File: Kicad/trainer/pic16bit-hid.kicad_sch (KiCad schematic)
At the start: 18 parts

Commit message: Update
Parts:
- BB401: renamed from BB?; value (none) -> BREADBOARD-170; footprint (none) -> tronixio:BREADBOARD-170
- EB401: value (none) -> EXPANSION-BOARD; footprint (none) -> tronixio:TRONIXIO-EXPANSION-BOARD
- JP401: value (none) -> VEE; footprint (none) -> tronixio:HARWIN-M20-999024x
- JP402: value (none) -> BCKL; footprint (none) -> tronixio:HARWIN-M20-999024x
- K401, K402: value (none) -> HARWIN-254-F-1X10-VERTICAL; footprint (none) -> tronixio:HARWIN-M20-782104x
- K409: value (none) -> HARWIN-254-F-1X16-VERTICAL; footprint (none) -> tronixio:HARWIN-M20-782164x
- LED401: value (none) -> KINGBRIGHT-DC10EWA; footprint (none) -> tronixio:KINGBRIGHT-DC
- P401: value (none) -> AN1; footprint (none) -> tronixio:PIHER-PT10MV
- P402: value (none) -> AN2; footprint (none) -> tronixio:PIHER-PT10MV
- R401: value (none) -> 5K; footprint (none) -> tronixio:PIHER-PT10LV
- R402: value (none) -> 10Ω; footprint (none) -> tronixio:RESISTOR-TH-1016
- RA401: value (none) -> 330Ω; footprint (none) -> tronixio:4611X
- S401: value (none) -> S1; footprint (none) -> tronixio:CK-KSA-TH
- S402: value (none) -> S3; footprint (none) -> tronixio:CK-KSA-TH
- S403: value (none) -> BOURNS-PEC12R-24DENTS; footprint (none) -> tronixio:BOURNS-PEC12R-SWITCH
- S404: value (none) -> S2; footprint (none) -> tronixio:CK-KSA-TH
- S405: value (none) -> S4; footprint (none) -> tronixio:CK-KSA-TH

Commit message: Update
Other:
- moved on the sheet: R401, R402

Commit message: Update Trainer
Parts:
- EB401: Name TRONIXIO-EXPANSION-BOARD -> (none)
- JP401, JP402: Name HARWIN-254-M-1X02-JUMPER-VERTICAL -> (none)
- K401, K402: Name HARWIN-254-F-1X10-VERTICAL -> (none)
- K409: Name HARWIN-254-F-1X16-VERTICAL -> (none)
- LED401: Name KINGBRIGHT-DC10EWA -> (none)
- P401, P402: Name PIHER-PT10MV-10K -> (none)
- R401: Name PIHER-PT10LV-5K -> (none)
- R402: Name RESISTOR-1016TH-10R -> (none)
- RA401: footprint tronixio:4611X -> tronixio:BOURNS-4611X; Name BOURNS-4611X-330R -> (none)
- S401, S402, S404, S405: Name CK-KSA -> (none)
- S403: Name BOURNS-PEC12R-24DENTS-SWITCH -> (none)

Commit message: Update
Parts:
- S403: symbol tronixio:BOURNS-PEC12R-24DENTS-SWITCH -> tronixio:BOURNS-PEC12R-24-DENTS-SWITCH
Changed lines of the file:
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@@
     )
   )
-  (symbol (lib_id "tronixio:BOURNS-PEC12R-24DENTS-SWITCH") (at 78.74 99.06 0) (unit 1)
+  (symbol (lib_id "tronixio:BOURNS-PEC12R-24-DENTS-SWITCH") (at 78.74 99.06 0) (unit 1)
     (in_bom yes) (on_board yes) (dnp no)
     (property "Reference" "S403" (at 78.74 88.265 0)

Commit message: Update
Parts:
- R401: footprint tronixio:PIHER-PT10LV -> tronixio:PIHER-PT10MV
- R402: symbol tronixio:RESISTOR-1016TH-10R -> tronixio:RESISTOR-1016TH-10R-5P
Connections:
- net GND: now also S403.5; no longer S403.4
- net S5: now also S403.4; no longer S403.5
- net VDD renamed +VDD
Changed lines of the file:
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@@
       (effects (font (size 1 1)) hide)
-    )
-    (property "Name" "GND" (at 71.12 64.77 0)
-      (effects (font (size 1.15 1.15)) hide)
     )
     (pin "1")
@@
     )
     (property "Mouser" "604-DC-10EWA" (at 144.78 91.44 0)
+      (effects (font (size 1 1)) hide)
+    )
+    (property "MOUSER" "" (at 144.78 81.28 0)
       (effects (font (size 1 1)) hide)
     )
@@
       (effects (font (size 1.15 1.15)) (justify right))
     )
-    (property "Footprint" "tronixio:PIHER-PT10LV" (at 208.28 55.88 0)
+    (property "Footprint" "tronixio:PIHER-PT10MV" (at 208.28 55.88 0)
       (effects (font (size 1 1)) hide)
     )
@@
       (effects (font (size 1 1)) hide)
     )
-    (property "Name" "GND" (at 83.82 128.27 0)
-      (effects (font (size 1.15 1.15)) hide)
-    )
     (pin "1")
     (instances
@@
     (property "Datasheet" "" (at 71.12 78.74 0)
       (effects (font (size 1 1)) hide)
-    )
-    (property "Name" "GND" (at 71.12 82.55 0)
-      (effects (font (size 1.15 1.15)) hide)
     )
     (pin "1")
@@
       (effects (font (size 1 1)) hide)
     )
-    (property "Datasheet" "https://www.harwin.com/products/M20-7821446/" (at 48.26 106.68 0)
+    (property "Datasheet" "https://www.harwin.com/products/M20-7821406/" (at 48.26 106.68 0)
       (effects (font (size 1 1)) hide)
     )
@@
       (effects (font (size 1 1)) hide)
     )
-    (property "Name" "GND" (at 88.9 82.55 0)
-      (effects (font (size 1.15 1.15)) hide)
-    )
     (pin "1")
     (instances
@@
       (effects (font (size 1 1)) hide)
     )
-    (property "Datasheet" "https://www.harwin.com/products/M20-9990846/" (at 220.98 93.98 0)
+    (property "Datasheet" "https://www.harwin.com/products/M20-9990246/" (at 220.98 93.98 0)
       (effects (font (size 1 1)) hide)
     )
@@
     )
   )
-  (symbol (lib_id "tronixio:POWER-VDD") (at 208.28 58.42 0) (unit 1)
+  (symbol (lib_id "tronixio:POWER-+VDD") (at 208.28 58.42 0) (unit 1)
     (in_bom yes) (on_board yes) (dnp no) (fields_autoplaced)
     (property "Reference" "#PWR0176" (at 208.28 68.58 0)
@@
       (effects (font (size 1 1)) hide)
     )
-    (property "Datasheet" "https://www.harwin.com/products/M20-9990846/" (at 218.44 93.98 0)
+    (property "Datasheet" "https://www.harwin.com/products/M20-9990246/" (at 218.44 93.98 0)
       (effects (font (size 1 1)) hide)
     )
@@
     )
   )
-  (symbol (lib_id "tronixio:POWER-VDD") (at 73.66 114.3 0) (unit 1)
+  (symbol (lib_id "tronixio:POWER-+VDD") (at 73.66 114.3 0) (unit 1)
     (in_bom yes) (on_board yes) (dnp no) (fields_autoplaced)
     (property "Reference" "#PWR0173" (at 73.66 124.46 0)
@@
       (effects (font (size 1 1)) hide)
     )
-    (property "Name" "GND" (at 208.28 78.74 0)
-      (effects (font (size 1.15 1.15)) hide)
-    )
     (pin "1")
     (instances
@@
       (effects (font (size 1 1)) hide)
     )
-    (property "Name" "GND" (at 88.9 128.27 0)
-      (effects (font (size 1.15 1.15)) hide)
-    )
     (pin "1")
     (instances
@@
       (effects (font (size 1 1)) hide)
     )
-    (property "Name" "GND" (at 88.9 64.77 0)
-      (effects (font (size 1.15 1.15)) hide)
-    )
     (pin "1")
     (instances
@@
     )
   )
-  (symbol (lib_id "tronixio:RESISTOR-1016TH-10R") (at 220.98 68.58 0) (unit 1)
+  (symbol (lib_id "tronixio:RESISTOR-1016TH-10R-5P") (at 220.98 68.58 0) (unit 1)
     (in_bom yes) (on_board yes) (dnp no)
     (property "Reference" "R402" (at 221.615 64.77 0)
@@
       (effects (font (size 1 1)) hide)
     )
-    (property "Name" "GND" (at 93.98 128.27 0)
-      (effects (font (size 1.15 1.15)) hide)
-    )
     (pin "1")
     (instances
@@
       (effects (font (size 1 1)) hide)
     )
-    (property "Datasheet" "https://www.harwin.com/products/M20-7821446/" (at 132.08 86.36 0)
+    (property "Datasheet" "https://www.harwin.com/products/M20-7821406/" (at 132.08 86.36 0)
       (effects (font (size 1 1)) hide)
     )
@@
       (effects (font (size 1 1)) hide)
     )
-    (property "Name" "GND" (at 73.66 128.27 0)
-      (effects (font (size 1.15 1.15)) hide)
-    )
     (pin "1")
     (instances
@@
     )
   )
-  (symbol (lib_id "tronixio:POWER-VDD") (at 83.82 114.3 0) (unit 1)
+  (symbol (lib_id "tronixio:POWER-+VDD") (at 83.82 114.3 0) (unit 1)
     (in_bom yes) (on_board yes) (dnp no) (fields_autoplaced)
     (property "Reference" "#PWR0168" (at 83.82 124.46 0)
@@
     (property "Datasheet" "" (at 167.64 82.55 0)
       (effects (font (size 1 1)) hide)
-    )
-    (property "Name" "GND" (at 167.64 86.36 0)
-      (effects (font (size 1.15 1.15)) hide)
     )
     (pin "1")
@@
       (effects (font (size 1 1)) hide)
     )
-    (property "Datasheet" "https://www.harwin.com/products/M20-7821446/" (at 208.28 132.08 0)
+    (property "Datasheet" "https://www.harwin.com/products/M20-7821646/" (at 208.28 132.08 0)
       (effects (font (size 1 1)) hide)
     )
@@
       (effects (font (size 1 1)) hide)
     )
-    (property "Name" "GND" (at 78.74 105.41 0)
-      (effects (font (size 1.15 1.15)) hide)
-    )
-    (pin "1")
+    (pin "1")

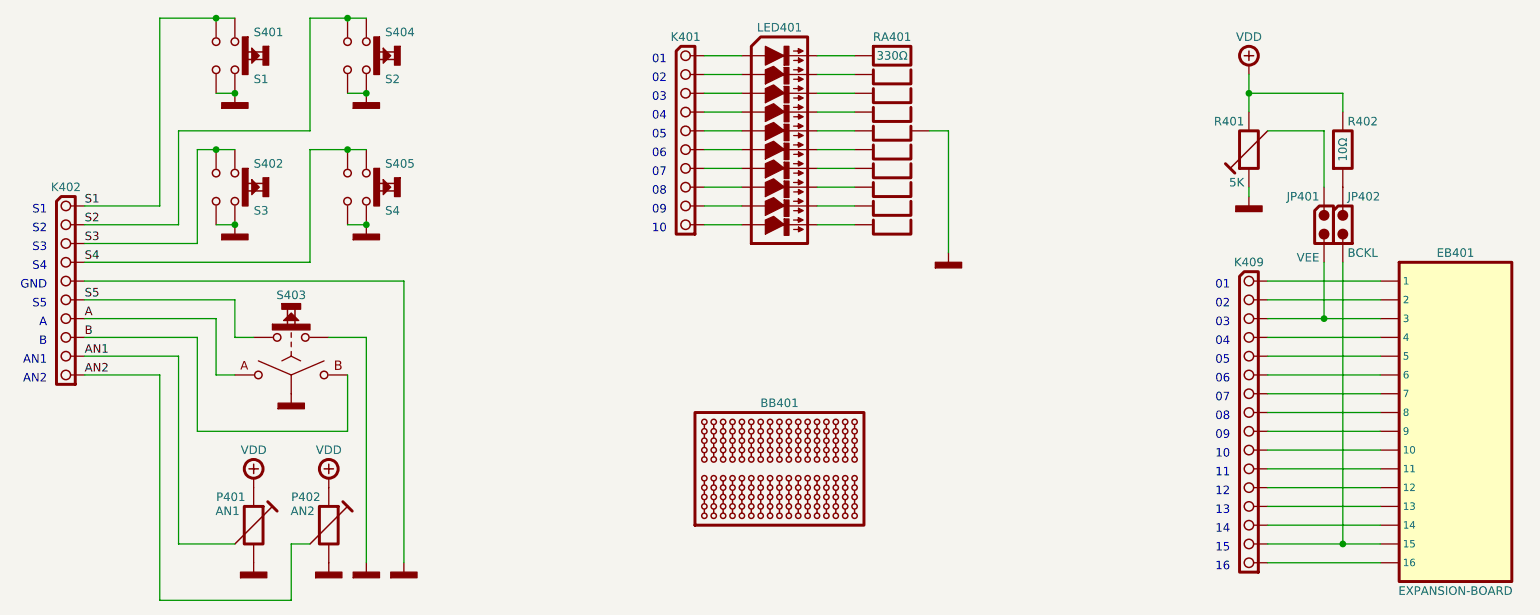
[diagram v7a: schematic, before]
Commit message: Update Trainer Kicad 8
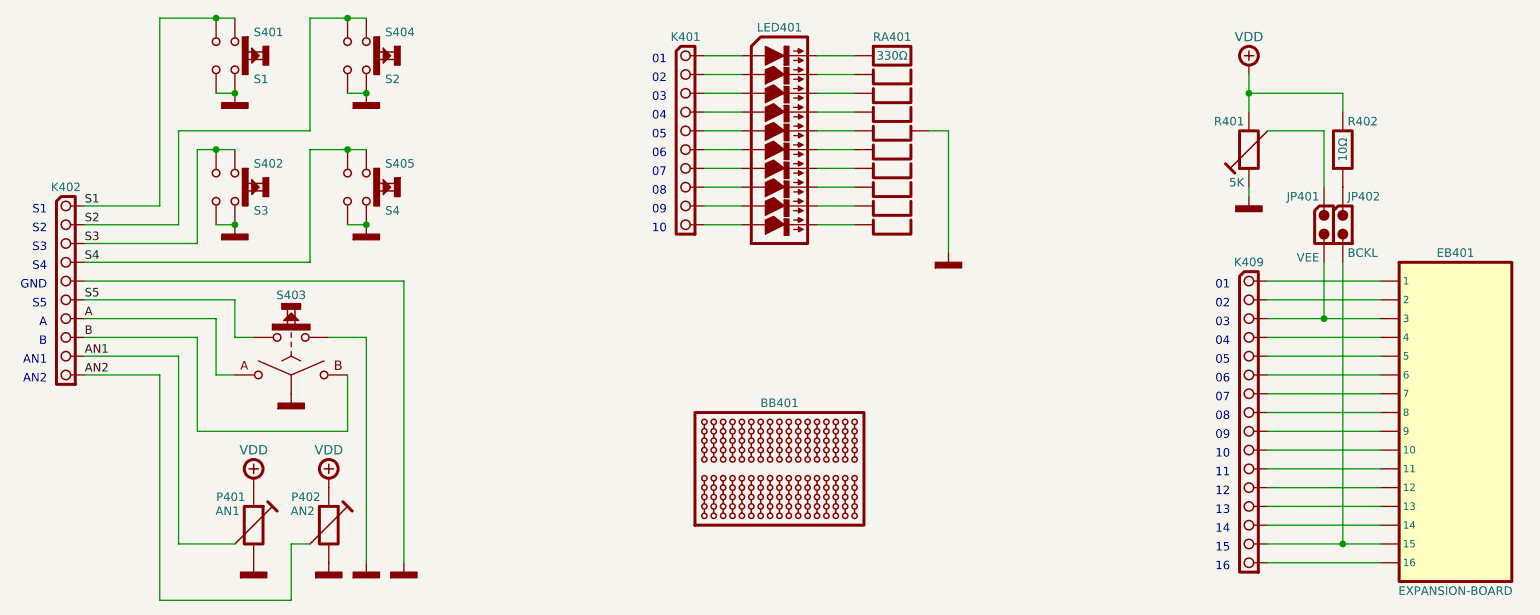
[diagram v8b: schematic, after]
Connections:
- net +VDD renamed POWER-VDD
- net GND renamed POWER-GND
